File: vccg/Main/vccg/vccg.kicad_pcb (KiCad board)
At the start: 2 copper layers, 50.8 x 103.4 mm, 45 parts, among them J1 MelodyClock, J10 melody, J11 oled, J2 ChordClock, J3 ChordCV, J4 OctaveCV, J5 MelodyCV, J6 Conn_02x05_Odd_Even, J7 root, J8 chord1, J9 chord2, Q1 2N3904, Q2 2N3904, SW1 Key_Up, SW2 Key_down, SW3 is_minor, U1 MCP6004, U2 LM7805_TO220, U3 MCP4728

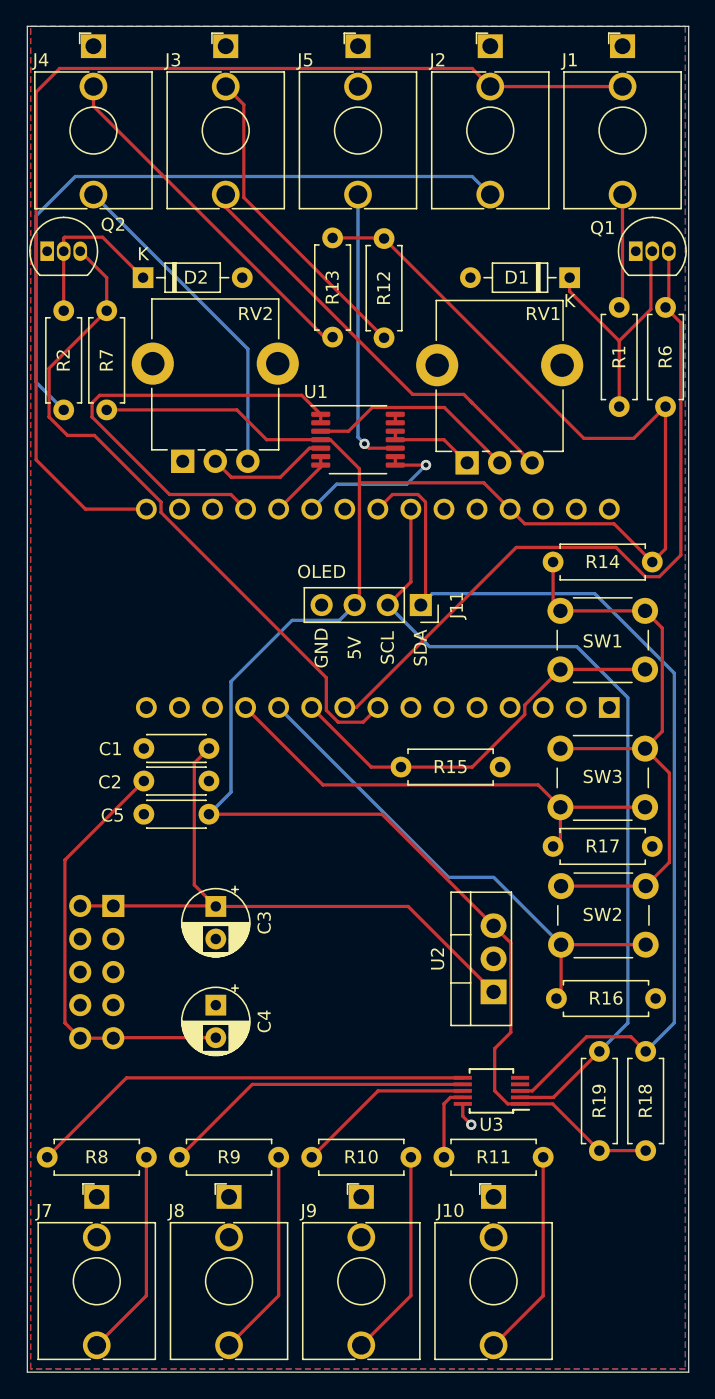
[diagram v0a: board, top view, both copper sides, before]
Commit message: Final pass
note, at least USB doesn't work at this state. I don't know what else
doesn't work. 3v3 power works, I can't speak to the rest.
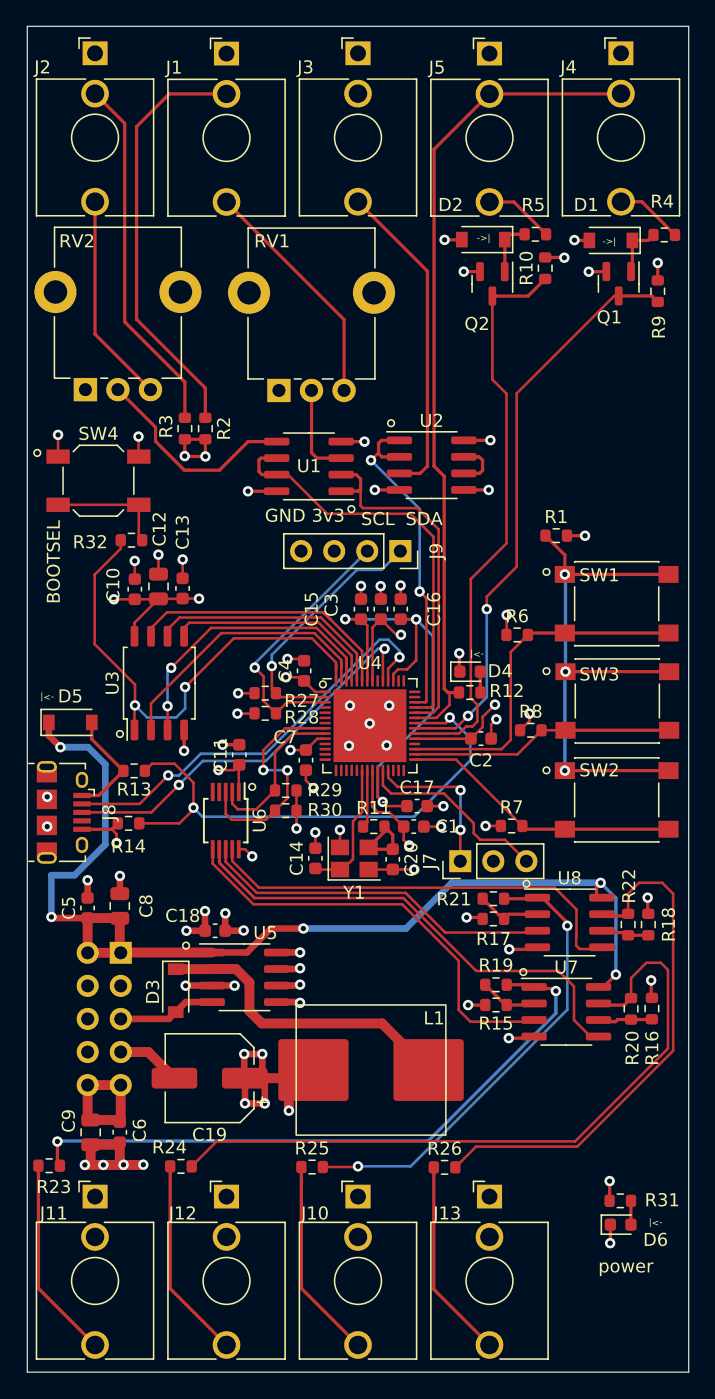
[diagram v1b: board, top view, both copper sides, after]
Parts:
- removed A1: Arduino_Nano_v3.x, Module:Arduino_Nano
- added C10: 100n, Capacitor_SMD:C_0603_1608Metric, F.Cu at (186.1, 67.4)
- added C11: 100n, Capacitor_SMD:C_0603_1608Metric, F.Cu at (194.1, 80.1)
- added C12: 2u2, Capacitor_SMD:C_0805_2012Metric, F.Cu at (187.9, 67.2)
- added C13: 100n, Capacitor_SMD:C_0603_1608Metric, F.Cu at (189.7, 67.3)
- added C14: 6pf, Capacitor_SMD:C_0603_1608Metric, F.Cu at (199.9, 88.0)
- added C15: 100n, Capacitor_SMD:C_0603_1608Metric, F.Cu at (203.4, 68.9)
- added C16: 100n, Capacitor_SMD:C_0603_1608Metric, F.Cu at (206.5, 68.9)
- added C17: 100n, Capacitor_SMD:C_0603_1608Metric, F.Cu at (207.7, 84.0)
- added C18: 100n, Capacitor_SMD:C_0603_1608Metric, F.Cu at (192.2, 93.6)
- added C19: 220uF, Capacitor_SMD:CP_Elec_6.3x7.7, F.Cu at (191.8, 104.9)
- added C20: 6pf, Capacitor_SMD:C_0603_1608Metric, F.Cu at (205.9, 88.1)
- added C6: 10n, Capacitor_SMD:C_0603_1608Metric, F.Cu at (184.9, 109.1)
- added C7: 100n, Capacitor_SMD:C_0603_1608Metric, F.Cu at (199.2, 80.5)
- added C8: 10u, Capacitor_SMD:C_0805_2012Metric, F.Cu at (184.9, 91.7)
- added C9: 10u, Capacitor_SMD:C_0805_2012Metric, F.Cu at (182.7, 109.1)
- added D3: B5819W, Diode_SMD:D_SOD-123, F.Cu at (189.2, 98.2)
- added D4: LED, Diode_SMD:D_0603_1608Metric, F.Cu at (211.8, 73.7)
- added D5: B5819W, Diode_SMD:D_SOD-123, F.Cu at (181.1, 77.6)
- added D6: LED, Diode_SMD:D_0603_1608Metric, F.Cu at (223.4, 116.2)
- added J12: chord1, Connector_Audio:Jack_3.5mm_QingPu_WQP-PJ398SM_Vertical_CircularHoles, F.Cu at (193.1, 114.0)
- added J13: melody, Connector_Audio:Jack_3.5mm_QingPu_WQP-PJ398SM_Vertical_CircularHoles, F.Cu at (213.3, 114.0)
- added L1: 68uh 2A, SynthStuff:Inductor_SMD-L_SMMS1040, F.Cu at (204.2, 104.3)
- added R20: 10K, Resistor_SMD:R_0603_1608Metric, F.Cu at (224.2, 99.6)
- added R21: 10K, Resistor_SMD:R_0603_1608Metric, F.Cu at (213.6, 91.1)
- added R22: 10K, Resistor_SMD:R_0603_1608Metric, F.Cu at (223.9, 93.1)
- added R23: 1K, Resistor_SMD:R_0603_1608Metric, F.Cu at (179.5, 111.7)
- added R24: 1K, Resistor_SMD:R_0603_1608Metric, F.Cu at (189.6, 111.7)
- added R25: 1K, Resistor_SMD:R_0603_1608Metric, F.Cu at (199.7, 111.8)
- added R26: 1K, Resistor_SMD:R_0603_1608Metric, F.Cu at (209.8, 111.8)
- added R27: 100K, Resistor_SMD:R_0603_1608Metric, F.Cu at (196.1, 75.3)
- added R28: 100K, Resistor_SMD:R_0603_1608Metric, F.Cu at (196.1, 76.9)
- added R29: 100K, Resistor_SMD:R_0603_1608Metric, F.Cu at (197.7, 82.8)
- added R3: 1K, Resistor_SMD:R_0603_1608Metric, F.Cu at (189.9, 55.0)
- added R30: 100K, Resistor_SMD:R_0603_1608Metric, F.Cu at (197.7, 84.4)
- added R31: 1K, Resistor_SMD:R_0603_1608Metric, F.Cu at (223.3, 114.3)
- added R32: 1K, Resistor_SMD:R_0603_1608Metric, F.Cu at (185.8, 63.6)
- added R4: 100K, Resistor_SMD:R_0603_1608Metric, F.Cu at (226.7, 40.1)
- added R5: 100K, Resistor_SMD:R_0603_1608Metric, F.Cu at (216.8, 40.1)
- added SW4: BOOT, Button_Switch_SMD:SW_SPST_SKQG_WithStem, F.Cu at (183.3, 59.0)
- added U4: RP2040, Package_DFN_QFN:QFN-56-1EP_7x7mm_P0.4mm_EP5.6x5.6mm, F.Cu at (204.1, 77.9)
- added U5: XL1509, Package_SO:SOIC-8_3.9x4.9mm_P1.27mm, F.Cu at (194.5, 97.2)
- added U6: MCP4728, Package_SO:MSOP-10_3x3mm_P0.5mm, F.Cu at (193.0, 85.1)
- added U7: LM2904, Package_SO:SOIC-8_3.9x4.9mm_P1.27mm, F.Cu at (219.2, 99.8)
- added U8: LM2904, Package_SO:SOIC-8_3.9x4.9mm_P1.27mm, F.Cu at (219.5, 93.0)
- added Y1: 12Mhz, Crystal:Crystal_SMD_3225-4Pin_3.2x2.5mm, F.Cu at (202.9, 88.0)
- C1, C2: value 10n -> 100n; footprint Capacitor_THT:C_Disc_D4.3mm_W1.9mm_P5.00mm -> Capacitor_SMD:C_0603_1608Metric
- C3, C4: value 10u -> 100n; footprint Capacitor_THT:CP_Radial_D5.0mm_P2.50mm -> Capacitor_SMD:C_0603_1608Metric
- C5: footprint Capacitor_THT:C_Disc_D4.3mm_W1.9mm_P5.00mm -> Capacitor_SMD:C_0603_1608Metric
- D1, D2: footprint Diode_THT:D_DO-35_SOD27_P7.62mm_Horizontal -> Diode_SMD:D_SOD-123
- J1: value MelodyClock -> ChordCV
- J10: value melody -> chord2
- J11: value oled -> root; footprint Connector_PinSocket_2.54mm:PinSocket_1x04_P2.54mm_Vertical -> Connector_Audio:Jack_3.5mm_QingPu_WQP-PJ398SM_Vertical_CircularHoles
- J2: value ChordClock -> OctaveCV
- J3: value ChordCV -> MelodyCV
- J4: value OctaveCV -> MelodyClock
- J5: value MelodyCV -> ChordClock
- J7: value root -> Conn_01x03_Male; footprint Connector_Audio:Jack_3.5mm_QingPu_WQP-PJ398SM_Vertical_CircularHoles -> Connector_PinHeader_2.54mm:PinHeader_1x03_P2.54mm_Vertical
- J8: value chord1 -> USB_B_Micro; footprint Connector_Audio:Jack_3.5mm_QingPu_WQP-PJ398SM_Vertical_CircularHoles -> Connector_USB:USB_Micro-B_Amphenol_10118194_Horizontal
- J9: value chord2 -> oled; footprint Connector_Audio:Jack_3.5mm_QingPu_WQP-PJ398SM_Vertical_CircularHoles -> Connector_PinSocket_2.54mm:PinSocket_1x04_P2.54mm_Vertical
- Q1, Q2: value 2N3904 -> MMBT3904; footprint Package_TO_SOT_THT:TO-92_Inline -> Package_TO_SOT_SMD:SOT-23
- R1, R15, R16, R17, R18, R19: value 100K -> 10K; footprint Resistor_THT:R_Axial_DIN0207_L6.3mm_D2.5mm_P7.62mm_Horizontal -> Resistor_SMD:R_0603_1608Metric
- R10, R9: value 1K -> 10K; footprint Resistor_THT:R_Axial_DIN0207_L6.3mm_D2.5mm_P7.62mm_Horizontal -> Resistor_SMD:R_0603_1608Metric
- R11, R12, R14: footprint Resistor_THT:R_Axial_DIN0207_L6.3mm_D2.5mm_P7.62mm_Horizontal -> Resistor_SMD:R_0603_1608Metric
- R13: value 1K -> 5K6; footprint Resistor_THT:R_Axial_DIN0207_L6.3mm_D2.5mm_P7.62mm_Horizontal -> Resistor_SMD:R_0603_1608Metric
- R2: value 100K -> 1K; footprint Resistor_THT:R_Axial_DIN0207_L6.3mm_D2.5mm_P7.62mm_Horizontal -> Resistor_SMD:R_0603_1608Metric
- R6, R7: value 10K -> 100K; footprint Resistor_THT:R_Axial_DIN0207_L6.3mm_D2.5mm_P7.62mm_Horizontal -> Resistor_SMD:R_0603_1608Metric
- R8: value 1K -> 100K; footprint Resistor_THT:R_Axial_DIN0207_L6.3mm_D2.5mm_P7.62mm_Horizontal -> Resistor_SMD:R_0603_1608Metric
- SW1, SW2, SW3: footprint Button_Switch_THT:SW_PUSH_6mm -> Button_Switch_SMD:SW_SPST_PTS645
- U1: value MCP6004 -> MCP6002-xSN; footprint Package_SO:TSSOP-14_4.4x5mm_P0.65mm -> Package_SO:SOIC-8_3.9x4.9mm_P1.27mm
- U2: value LM7805_TO220 -> MCP6002-xSN; footprint Package_TO_SOT_THT:TO-220-3_Vertical -> Package_SO:SOIC-8_3.9x4.9mm_P1.27mm
- U3: value MCP4728 -> W25Q16JV; footprint Package_SO:MSOP-10_3x3mm_P0.5mm -> Package_SO:SOIC-8_5.275x5.275mm_P1.27mm
- moved R9 72.6 mm to (226.2, 44.5), turned to 90 degrees
- moved R10 69.1 mm to (217.6, 42.7), turned to 90 degrees
- moved J11 51.9 mm to (183.0, 114.0), turned to 0 degrees
- moved R7 50.3 mm to (215.0, 85.5), turned to 0 degrees
- moved J9 49.7 mm to (206.5, 64.4), turned to -90 degrees
- moved R8 44.1 mm to (216.5, 78.2), turned to 0 degrees
- moved U2 40.7 mm to (208.9, 57.8), turned to 0 degrees
- moved J4 40.5 mm to (223.4, 26.2)
- moved U3 40.4 mm to (187.9, 74.6), turned to 90 degrees
- moved R14 38.3 mm to (185.6, 85.3)
- moved J7 38.0 mm to (211.1, 88.3), turned to 90 degrees
- moved R13 36.6 mm to (186.0, 81.3), turned to 180 degrees
- moved Q2 34.3 mm to (213.5, 43.9), turned to -90 degrees
- moved J8 32.1 mm to (180.6, 84.5), turned to -90 degrees
- moved J1 30.4 mm to (193.1, 26.2)
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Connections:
- C1 pad 1: +12V -> +3V3
- C2 pad 1: GND -> +3V3
- C2 pad 2: -12V -> GND
- C3 pad 1: +12V -> +3V3
- C4 pad 1: GND -> +3V3
- C4 pad 2: -12V -> GND
- C5 pad 1: +5V -> +12V
- J1 pad TN: defaultClock -> Net-(J1-PadTN)
- J10 pad TN: (no net) -> unconnected-(J10-PadTN)
- J2 pad TN: defaultClock -> Net-(J2-PadTN)
- J3 pad TN: Net-(J3-PadTN) -> GND
- J4 pad TN: Net-(J4-PadTN) -> defaultClock
- J5 pad TN: (no net) -> defaultClock
- Q1 pad 1: GND -> Net-(D1-Pad1)
- Q1 pad 2: Net-(D1-Pad1) -> GND
- Q2 pad 1: GND -> Net-(D2-Pad1)
- Q2 pad 2: Net-(D2-Pad1) -> GND
- R1 pad 1: Net-(D1-Pad1) -> Net-(R1-Pad1)
- R1 pad 2: Net-(J1-PadT) -> +3V3
- R10 pad 1: Net-(J9-PadT) -> chordClock
- R10 pad 2: chord2 -> +3V3
- R11 pad 1: Net-(J10-PadT) -> XOUT
- R11 pad 2: quant -> Net-(C20-Pad1)
- R12 pad 1: Net-(J3-PadTN) -> Net-(D4-Pad2)
- R12 pad 2: +5V -> defaultClock
- R13 pad 1: Net-(J4-PadTN) -> GPIO_24
- R13 pad 2: +5V -> Net-(D5-Pad2)
- R14 pad 1: Net-(R14-Pad1) -> GND
- R14 pad 2: +5V -> GPIO_24
- R15 pad 1: GND -> Net-(R15-Pad1)
- R15 pad 2: key_up -> GND
- R16 pad 1: GND -> Net-(R16-Pad1)
- R16 pad 2: key_down -> GND
- R17 pad 1: GND -> Net-(R17-Pad1)
- R17 pad 2: is_minor -> GND
- R18 pad 1: SDA -> Net-(R18-Pad1)
- R18 pad 2: +5V -> GND
- R19 pad 1: SCL -> Net-(R19-Pad1)
- R19 pad 2: +5V -> Net-(R15-Pad1)
- R2 pad 1: Net-(D2-Pad1) -> Net-(J1-PadTN)
- R2 pad 2: Net-(J2-PadT) -> +3V3
- R6 pad 1: melodyClock -> GND
- R6 pad 2: +5V -> key_up
- R7 pad 1: chordClock -> GND
- R7 pad 2: +5V -> key_down
- R8 pad 1: Net-(J7-PadT) -> GND
- R8 pad 2: root -> is_minor
- R9 pad 1: Net-(J8-PadT) -> melodyClock
- R9 pad 2: chord1 -> +3V3
- RV1 pad 3: Net-(J3-PadT) -> Net-(J1-PadT)
- RV2 pad 3: Net-(J4-PadT) -> Net-(J2-PadT)
- SW1 pad 1: Net-(R14-Pad1) -> Net-(R1-Pad1)
- SW2 pad 1: Net-(R14-Pad1) -> Net-(R1-Pad1)
- SW3 pad 1: Net-(R14-Pad1) -> Net-(R1-Pad1)
- U1 pad 4: +5V -> GND
- U1 pad 8: melody -> +3V3
- U2 pad 1: +12V -> melody
- U2 pad 2: GND -> melody
- U2 pad 3: +5V -> Net-(J3-PadT)
- U3 pad 1: +5V -> QSPI_SS
- U3 pad 2: SCL -> QSPI_SD1
- U3 pad 3: SDA -> QSPI_SD2
- U3 pad 4: (no net) -> GND
- U3 pad 5: (no net) -> QSPI_SD0
- U3 pad 6: root -> QSPI_CLK
- U3 pad 7: chord1 -> QSPI_SD3
- U3 pad 8: chord2 -> +3V3
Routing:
- net +5V: track 177.7 -> 0.00 mm
- net +3V3: track 0.00 -> 90.9 mm, vias 0 -> 28
- net GND: track 8.78 -> 94.5 mm, vias 1 -> 57
- net SDA: track 76.6 -> 0.00 mm
- net SCL: track 65.1 -> 0.00 mm
- net Net-(R20-Pad1): track 0.00 -> 54.3 mm
- net Net-(R19-Pad1): track 0.00 -> 50.0 mm, vias 0 -> 2
- net Net-(R14-Pad1): track 47.3 -> 0.00 mm
- net Net-(R1-Pad1): track 0.00 -> 42.6 mm, vias 0 -> 3
- net GPIO_24: track 0.00 -> 41.5 mm, vias 0 -> 2
- net Net-(R22-Pad1): track 0.00 -> 40.7 mm
- net +1V1: track 0.00 -> 39.9 mm, vias 0 -> 3
- net QSPI_SS: track 0.00 -> 38.6 mm, vias 0 -> 2
- net Net-(R21-Pad1): track 0.00 -> 36.7 mm, vias 0 -> 2
- net Net-(J2-PadT): track 52.5 -> 16.2 mm
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- added copper zone on In2.Cu, net +3V3
- added copper zone on In1.Cu, net GND
- removed copper zone on B.Cu, net GND
- removed copper zone on F.Cu, net GND
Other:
- copper layers 2 -> 4
- net class Default removed
- board text added: "-12V______________"
- board text added: "->|"
- board text added: "3v3"
- board text added: "BOOTSEL"
- board text added: "Gray Noise Audio"
- board text added: "SDIO"
- board text added: "SWCLK"
- board text added: "VCCG v0.2"
- board text added: "power"
- board text removed: "-12V"
- board text removed: "5V"
- board text removed: "OLED"
- board text removed: "Voltage Controlled Chord Generator"
- board text removed: "v0.2"
